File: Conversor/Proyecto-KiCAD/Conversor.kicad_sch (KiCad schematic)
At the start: 35 parts, among them J2 ConnPila, J3 ConnTrafoP, J4 ConnTrafoS, J5 ConnLf, J6 ConnCarga, Q1 IRFP150, Q2 IRFP150, Q3 IRFP150, Q4 IRFP150

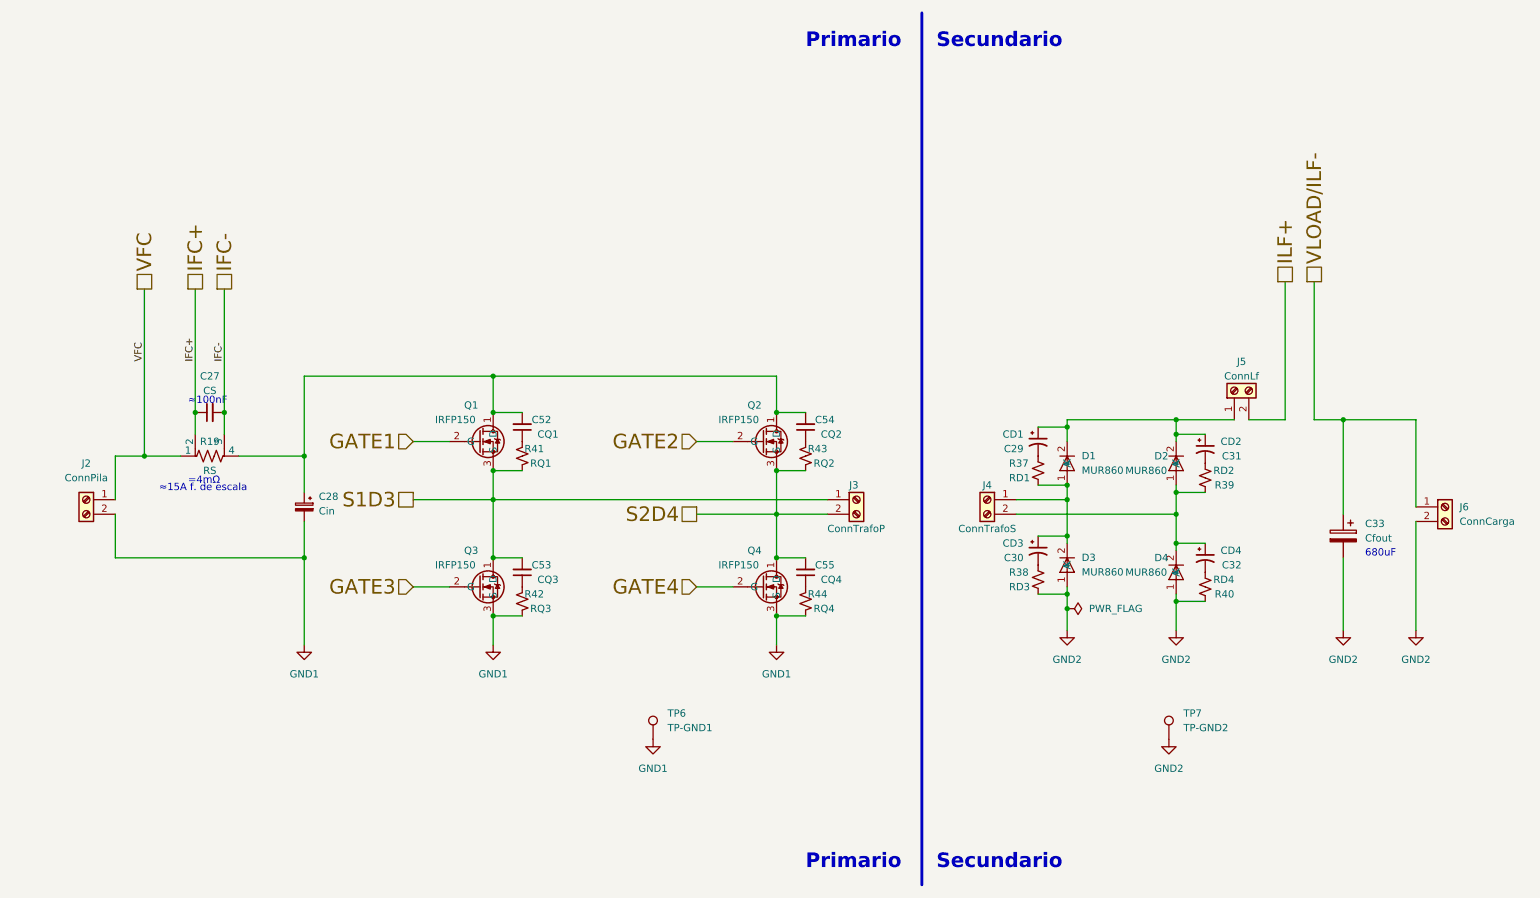
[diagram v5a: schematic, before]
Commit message: Agregar resistencias de pull-up faltantes
- Agregar resistencias de pull-up a la salida de cada inversor del
74LS06
- Crear plano de U5V en la capa superior alrededor del FTDI
- Ponerle los valores a los componentes para poder generar correctamente
el BOM (Bill of Materials)
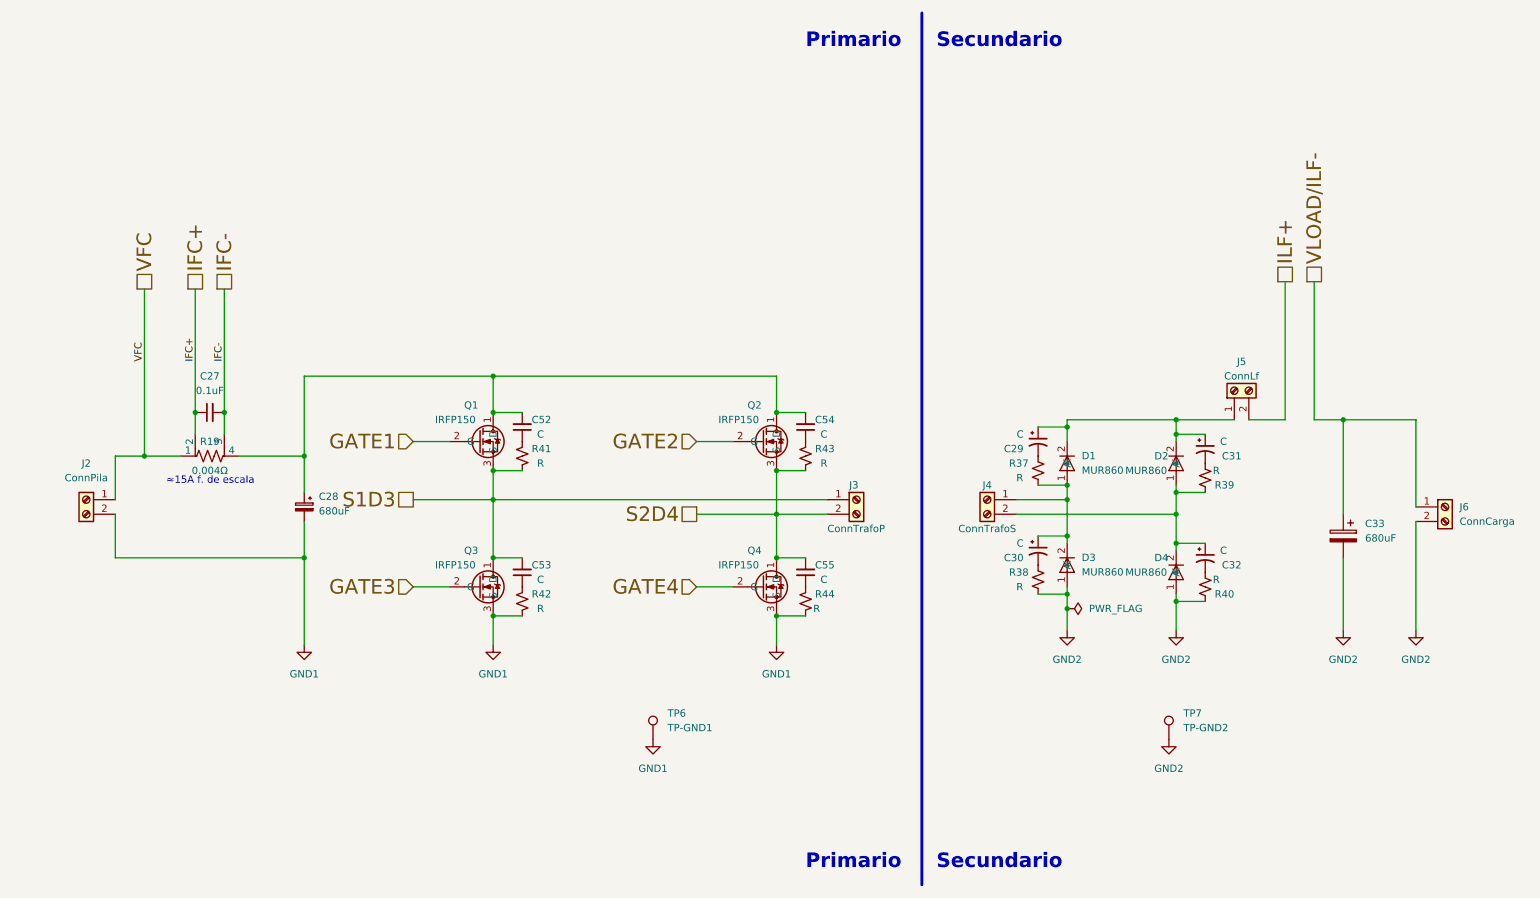
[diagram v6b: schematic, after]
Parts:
- C27: value CS -> 0.1uF
- C28: value Cin -> 680uF
- C29: value CD1 -> C
- C30: value CD3 -> C
- C31: value CD2 -> C
- C32: value CD4 -> C
- C33: value Cfout -> 680uF
- C52: value CQ1 -> C
- C53: value CQ3 -> C
- C54: value CQ2 -> C
- C55: value CQ4 -> C
- R19: value RS -> 0.004Ω
- R37: value RD1 -> R
- R38: value RD3 -> R
- R39: value RD2 -> R
- R40: value RD4 -> R
- R41: value RQ1 -> R
- R42: value RQ3 -> R
- R43: value RQ2 -> R
- R44: value RQ4 -> R
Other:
- note removed: "680uF"
- note removed: "=4mΩ"
- note removed: "≈100nF"
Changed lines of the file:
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@@
     (stroke (width 0) (type default) (color 0 0 0 0))
-  )
-  (text "=4mΩ" (at 50.8 95.25 0)
-    (effects (font (size 1.27 1.27)) (justify left bottom))
   )
   (text "Secundario" (at 181.61 162.56 0)
@@
     (effects (font (size 2.54 2.54) (thickness 0.508) bold) (justify left bottom))
   )
-  (text "680uF" (at 256.54 107.95 0)
-    (effects (font (size 1.27 1.27)) (justify left bottom))
-  )
-  (text "≈15A f. de escala" (at 45.72 96.52 0)
+  (text "≈15A f. de escala" (at 46.99 95.25 0)
     (effects (font (size 1.27 1.27)) (justify left bottom))
   )
@@
     (effects (font (size 2.54 2.54) (thickness 0.508) bold) (justify left bottom))
   )
-  (text "≈100nF" (at 50.8 81.28 0)
-    (effects (font (size 1.27 1.27)) (justify left bottom))
-  )
   (text "Primario" (at 158.75 19.05 0)
     (effects (font (size 2.54 2.54) (thickness 0.508) bold) (justify left bottom))
@@
       (effects (font (size 1.27 1.27)) (justify right))
     )
-    (property "Value" "CD3" (id 1) (at 196.85 105.41 0)
+    (property "Value" "C" (id 1) (at 196.85 105.41 0)
       (effects (font (size 1.27 1.27)) (justify right))
     )
@@
       (effects (font (size 1.27 1.27)) (justify right))
     )
-    (property "Value" "CD1" (id 1) (at 196.85 86.36 0)
+    (property "Value" "C" (id 1) (at 196.85 86.36 0)
       (effects (font (size 1.27 1.27)) (justify right))
     )
@@
   (symbol (lib_id "Device:R_Small_US") (at 158.75 115.57 0) (mirror x) (unit 1)
     (in_bom yes) (on_board yes)
-    (property "Reference" "R44" (id 0) (at 162.56 114.3 0)
-      (effects (font (size 1.27 1.27)) (justify right))
-    )
-    (property "Value" "RQ4" (id 1) (at 163.83 116.84 0)
+    (property "Reference" "R44" (id 0) (at 163.83 114.3 0)
+      (effects (font (size 1.27 1.27)) (justify right))
+    )
+    (property "Value" "R" (id 1) (at 161.29 116.84 0)
       (effects (font (size 1.27 1.27)) (justify right))
     )
@@
       (effects (font (size 1.27 1.27)) (justify right))
     )
-    (property "Value" "Cin" (id 1) (at 73.66 99.7838 0)
+    (property "Value" "680uF" (id 1) (at 73.66 99.7838 0)
       (effects (font (size 1.27 1.27)) (justify right))
     )
@@
       (effects (font (size 1.27 1.27)) (justify right))
     )
-    (property "Value" "CQ4" (id 1) (at 165.1 111.76 0)
+    (property "Value" "C" (id 1) (at 162.56 111.76 0)
       (effects (font (size 1.27 1.27)) (justify right))
     )
@@
       (effects (font (size 1.27 1.27)) (justify right))
     )
-    (property "Value" "CQ3" (id 1) (at 115.57 111.76 0)
+    (property "Value" "C" (id 1) (at 113.03 111.76 0)
       (effects (font (size 1.27 1.27)) (justify right))
     )
@@
   (symbol (lib_id "Device:R_Small_US") (at 109.22 115.57 0) (mirror x) (unit 1)
     (in_bom yes) (on_board yes)
-    (property "Reference" "R42" (id 0) (at 113.03 114.3 0)
-      (effects (font (size 1.27 1.27)) (justify right))
-    )
-    (property "Value" "RQ3" (id 1) (at 114.3 116.84 0)
+    (property "Reference" "R42" (id 0) (at 114.3 114.3 0)
+      (effects (font (size 1.27 1.27)) (justify right))
+    )
+    (property "Value" "R" (id 1) (at 113.03 116.84 0)
       (effects (font (size 1.27 1.27)) (justify right))
     )
@@
   (symbol (lib_id "Device:R_Small_US") (at 109.22 90.17 0) (mirror x) (unit 1)
     (in_bom yes) (on_board yes)
-    (property "Reference" "R41" (id 0) (at 113.03 88.9 0)
-      (effects (font (size 1.27 1.27)) (justify right))
-    )
-    (property "Value" "RQ1" (id 1) (at 114.3 91.44 0)
+    (property "Reference" "R41" (id 0) (at 114.3 88.9 0)
+      (effects (font (size 1.27 1.27)) (justify right))
+    )
+    (property "Value" "R" (id 1) (at 113.03 91.44 0)
       (effects (font (size 1.27 1.27)) (justify right))
     )
@@
       (effects (font (size 1.27 1.27)) (justify right))
     )
-    (property "Value" "RD1" (id 1) (at 194.31 93.98 0)
+    (property "Value" "R" (id 1) (at 195.58 93.98 0)
       (effects (font (size 1.27 1.27)) (justify right))
     )
@@
       (effects (font (size 1.27 1.27)) (justify right))
     )
-    (property "Value" "CQ2" (id 1) (at 165.1 86.36 0)
+    (property "Value" "C" (id 1) (at 162.56 86.36 0)
       (effects (font (size 1.27 1.27)) (justify right))
     )
@@
       (effects (font (size 1.27 1.27)) (justify right))
     )
-    (property "Value" "CD2" (id 1) (at 234.95 87.63 0)
+    (property "Value" "C" (id 1) (at 232.41 87.63 0)
       (effects (font (size 1.27 1.27)) (justify right))
     )
@@
     (in_bom yes) (on_board yes) (fields_autoplaced)
     (property "Reference" "C27" (id 0) (at 54.6163 76.2 90))
-    (property "Value" "CS" (id 1) (at 54.6163 78.74 90))
+    (property "Value" "0.1uF" (id 1) (at 54.6163 78.74 90))
     (property "Footprint" "Capacitor_SMD:C_1206_3216Metric_Pad1.33x1.80mm_HandSolder" (id 2) (at 54.61 82.55 0)
       (effects (font (size 1.27 1.27)) hide)
@@
     (in_bom yes) (on_board yes)
     (property "Reference" "R19" (id 0) (at 54.61 87.63 90))
-    (property "Value" "RS" (id 1) (at 54.61 92.71 90))
+    (property "Value" "0.004Ω" (id 1) (at 54.61 92.71 90))
     (property "Footprint" "Resistor_SMD:R_Shunt_Vishay_WSK2512_6332Metric_T2.21mm" (id 2) (at 54.61 91.948 90)
       (effects (font (size 1.27 1.27)) hide)
@@
       (effects (font (size 1.27 1.27)) (justify right))
     )
-    (property "Value" "CQ1" (id 1) (at 115.57 86.36 0)
+    (property "Value" "C" (id 1) (at 113.03 86.36 0)
       (effects (font (size 1.27 1.27)) (justify right))
     )
@@
   (symbol (lib_id "Device:R_Small_US") (at 158.75 90.17 0) (mirror x) (unit 1)
     (in_bom yes) (on_board yes)
-    (property "Reference" "R43" (id 0) (at 162.56 88.9 0)
-      (effects (font (size 1.27 1.27)) (justify right))
-    )
-    (property "Value" "RQ2" (id 1) (at 163.83 91.44 0)
+    (property "Reference" "R43" (id 0) (at 163.83 88.9 0)
+      (effects (font (size 1.27 1.27)) (justify right))
+    )
+    (property "Value" "R" (id 1) (at 162.56 91.44 0)
       (effects (font (size 1.27 1.27)) (justify right))
     )
@@
       (effects (font (size 1.27 1.27)) (justify right))
     )
-    (property "Value" "RD4" (id 1) (at 233.68 111.76 0)
+    (property "Value" "R" (id 1) (at 231.14 111.76 0)
       (effects (font (size 1.27 1.27)) (justify right))
     )
@@
       (effects (font (size 1.27 1.27)) (justify right))
     )
-    (property "Value" "RD3" (id 1) (at 194.31 113.03 0)
+    (property "Value" "R" (id 1) (at 195.58 113.03 0)
       (effects (font (size 1.27 1.27)) (justify right))
     )
@@
       (effects (font (size 1.27 1.27)) (justify right))
     )
-    (property "Value" "RD2" (id 1) (at 233.68 92.71 0)
+    (property "Value" "R" (id 1) (at 231.14 92.71 0)
       (effects (font (size 1.27 1.27)) (justify right))
     )
@@
       (effects (font (size 1.27 1.27)) (justify right))
     )
-    (property "Value" "Cfout" (id 1) (at 256.54 104.5209 0)
+    (property "Value" "680uF" (id 1) (at 256.54 104.5209 0)
       (effects (font (size 1.27 1.27)) (justify right))
     )
@@
       (effects (font (size 1.27 1.27)) (justify right))
     )
-    (property "Value" "CD4" (id 1) (at 234.95 106.68 0)
-      (effects (font (size 1.27 1.27)) (justify right))
-    )
+    (property "Value" "C" (id 1) (at 232.41 106.68 0)
+      (effects (font (size 1.27 1.27)) (justify right))
+    )

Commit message: Eliminar resistencias de pull-up de SCL y SDAI
- Se pueden remover las Rpu del lado del sensor ya que las Rpu de esas
lineas estan del otro lado (la barrera de aislación proteje de daños).
La de SDAO tiene que quedar por la salida open-drain del LM5056.
- También cambiar las Rpu de 10k a 4k7, porque la capacidad del bus es
muy baja (un solo esclavo y pistas cortas). Así se disminuye es rise
time (Rpu*Cbus) a la mitad.
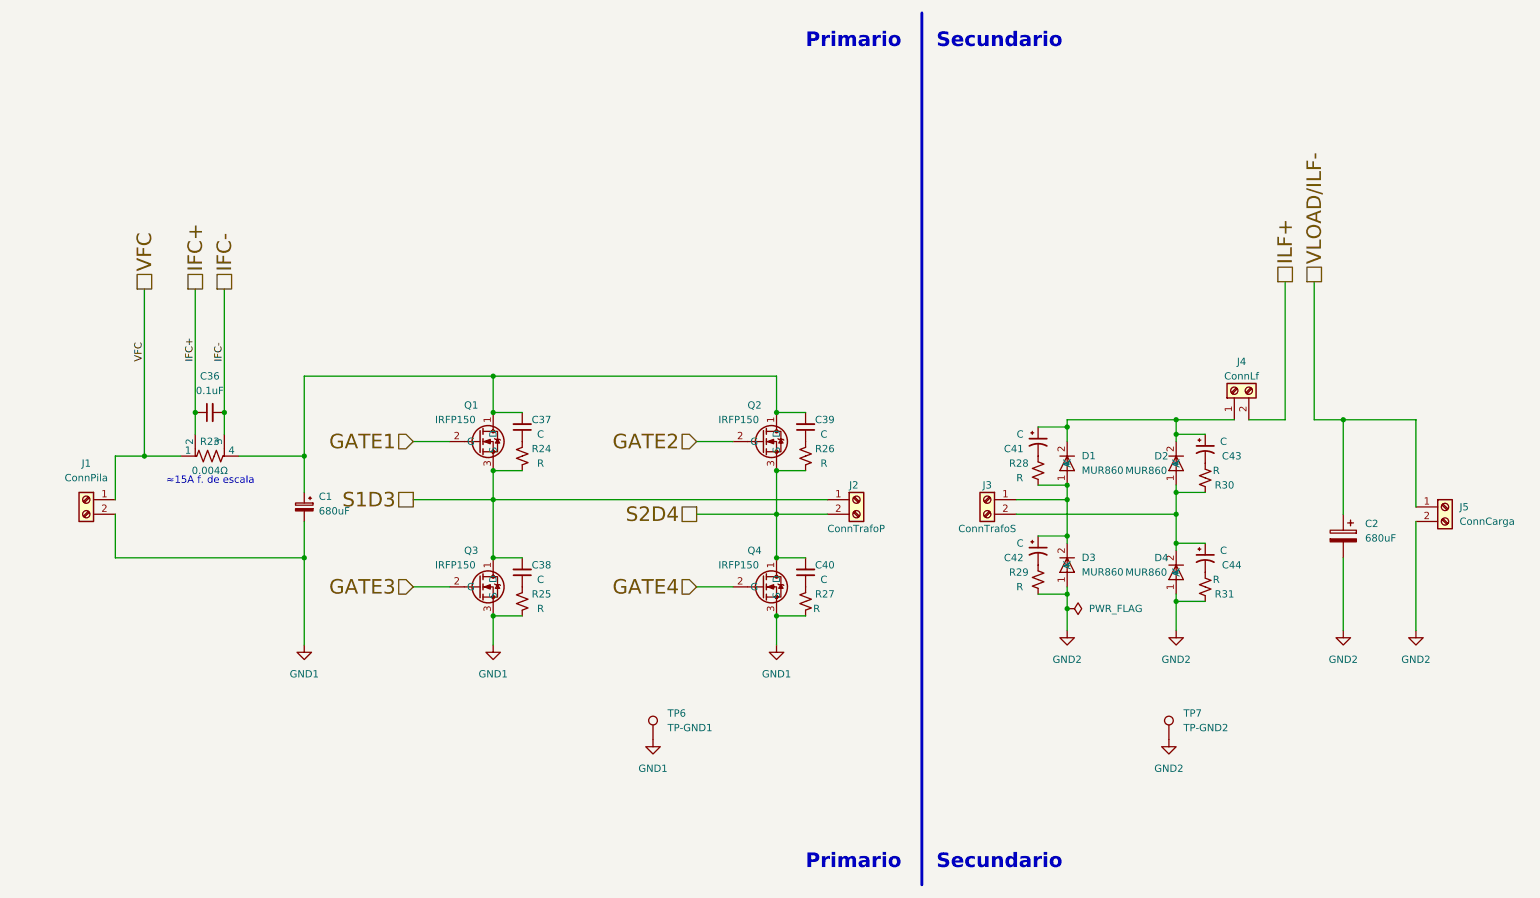
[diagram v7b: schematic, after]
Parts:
- renumbered C28 to C1, C33 to C2, C27 to C36, C52 to C37, C53 to C38, C54 to C39, C55 to C40, C29 to C41, C30 to C42, C31 to C43, C32 to C44, J2 to J1, J3 to J2, J4 to J3, J5 to J4, J6 to J5, R19 to R23, R41 to R24, R42 to R25, R43 to R26, R44 to R27, R37 to R28, R38 to R29, R39 to R30, R40 to R31

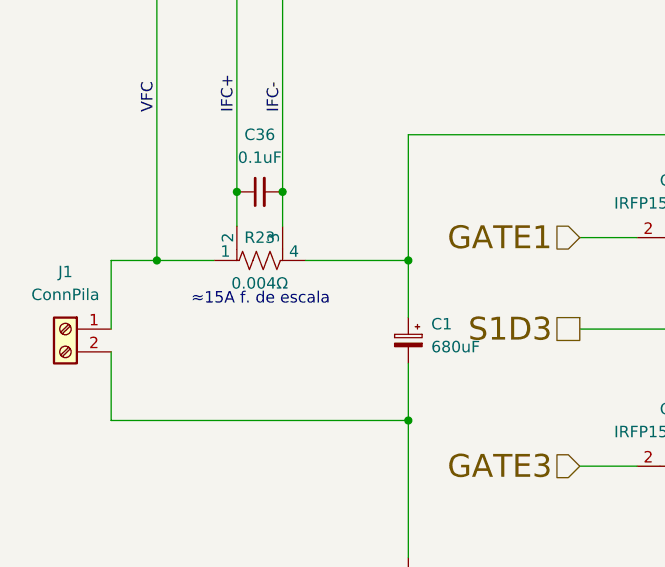
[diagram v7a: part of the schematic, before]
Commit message: Arreglar los primeros dos items marcados por Jorge
- Usar EPWM1A/B y EPWM2A/B para poder usar la función de phase-shift de
los modulos PWM y ahorrarse la sincronización manual
- Agregar diodos de descarga D8 y D9 a la salida de los drivers
- Agregar el Technical Reference Manual del DSP a la bibliografía
(descripción ultra detallada de todas las funciones del DSP)
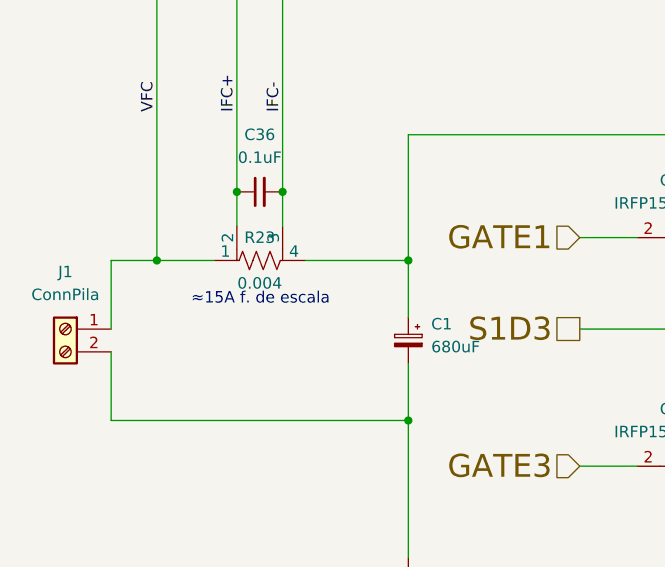
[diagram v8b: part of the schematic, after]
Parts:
- R23: value 0.004Ω -> 0.004
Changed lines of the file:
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@@
     (in_bom yes) (on_board yes)
     (property "Reference" "R23" (id 0) (at 54.61 87.63 90))
-    (property "Value" "0.004Ω" (id 1) (at 54.61 92.71 90))
+    (property "Value" "0.004" (id 1) (at 54.61 92.71 90))
     (property "Footprint" "Resistor_SMD:R_Shunt_Vishay_WSK2512_6332Metric_T2.21mm" (id 2) (at 54.61 91.948 90)
       (effects (font (size 1.27 1.27)) hide)
